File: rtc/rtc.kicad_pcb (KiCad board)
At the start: 2 copper layers, 40.4 x 36.5 mm, 14 parts, among them J1 Conn_02x03_Odd_Even, J2 Conn_01x04, J3 Conn_01x04, J4 Conn_01x04, U1 PCF8563T/5_518, Y1 LFXTAL016178REEL

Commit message: rtc pcb iteration 2
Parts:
- C1, C3: value C -> 24p; moved to B.Cu
- C2, D2, R1, R2, R3, U1, Y1: moved to B.Cu
- J1: footprint Connector_PinHeader_2.54mm:PinHeader_2x03_P2.54mm_Vertical -> Connector_PinSocket_2.54mm:PinSocket_2x03_P2.54mm_Vertical; moved to B.Cu
- J2, J3, J4: footprint pcb_footprints:JST_SH_BM04B-SRSS-TB_1x04-1MP_P1.00mm_Vertical -> pcb_footprints:SM04BSRSSTB; moved to B.Cu
- moved C3 87.7 mm to (152.3, 76.1), turned to 135 degrees
- moved C1 84.2 mm to (147.0, 81.1), turned to 135 degrees
- moved Y1 83.6 mm to (148.0, 77.0), turned to 135 degrees
- moved U1 80.7 mm to (155.9, 82.2), turned to -45 degrees
- moved R1 78.2 mm to (161.4, 93.3), turned to -135 degrees
- moved C2 74.5 mm to (156.6, 89.6)
- moved SUPERCAP1 72.1 mm to (161.6, 88.5), turned to -45 degrees
- moved D2 71.2 mm to (157.9, 92.9), turned to -135 degrees
- moved R2 69.3 mm to (152.0, 89.0), turned to -90 degrees
- moved R3 69.2 mm to (154.5, 89.0), turned to -90 degrees
- moved J2 64.1 mm to (160.0, 70.7), turned to 0 degrees
- moved J3 62.8 mm to (161.2, 78.3)
- moved J1 62.5 mm to (154.5, 98.5)
- moved J4 53.2 mm to (150.8, 70.7), turned to 0 degrees
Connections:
- J1 pad 1: +3.3V -> GND
- J1 pad 2: unconnected-(J1-Pin_2-Pad2) -> scl
- J1 pad 3: sda -> unconnected-(J1-Pin_3-Pad3)
- J1 pad 4: unconnected-(J1-Pin_4-Pad4) -> sda
- J1 pad 5: scl -> unconnected-(J1-Pin_5-Pad5)
- J1 pad 6: GND -> +3.3V
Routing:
- net GND: track 0.00 -> 71.1 mm, vias 2 -> 9
- net Net-(SUPERCAP1-+): track 18.3 -> 4.40 mm
- net sda: track 52.1 -> 44.9 mm, vias 3 -> 0
- net Net-(U1-OSCI): track 11.1 -> 6.65 mm
- net scl: track 50.6 -> 47.8 mm, vias 5 -> 0
- net Net-(U1-OSCO): track 7.89 -> 6.35 mm
- net +3.3V: track 55.1 -> 54.9 mm, vias 3 -> 4
- removed copper zone on F.Cu, net GND
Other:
- board size 40.4 x 36.5 mm -> 23.5 x 32.4 mm
- board text removed: "3V3"
- board text removed: "GND"
- board text removed: "SCL"
- board text removed: "SDA"

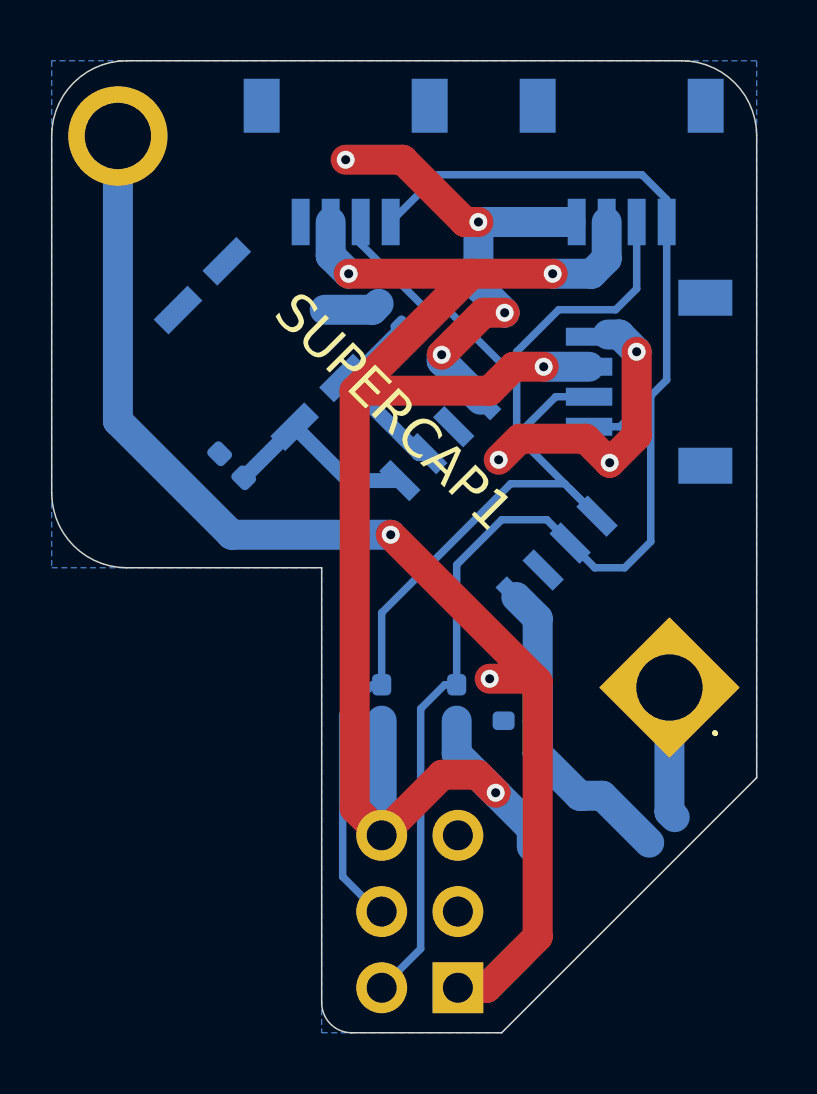
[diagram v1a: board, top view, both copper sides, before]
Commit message: finished rtc board + sensor base 3d model change
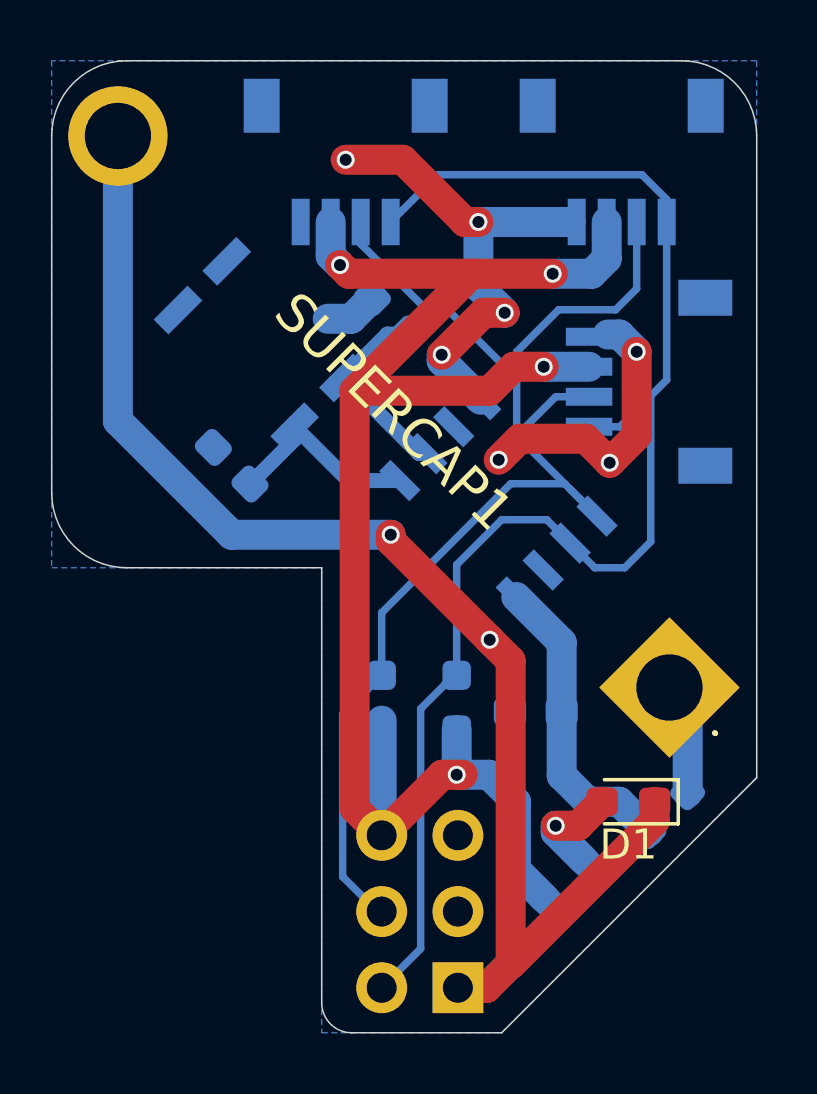
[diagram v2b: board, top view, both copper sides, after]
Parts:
- added D1: LED, LED_SMD:LED_0603_1608Metric_Pad1.05x0.95mm_HandSolder, F.Cu at (160.2, 92.3)
- added G***: LOGO, LOGO, B.Cu at (143.2, 79.7)
- added R4: 2.5k, Resistor_SMD:R_0603_1608Metric_Pad0.98x0.95mm_HandSolder, B.Cu at (158.1, 94.9)
- C1, C2, C3: footprint Capacitor_SMD:C_0402_1005Metric_Pad0.74x0.62mm_HandSolder -> Capacitor_SMD:C_0603_1608Metric_Pad1.08x0.95mm_HandSolder
- R1, R2, R3: footprint Resistor_SMD:R_0402_1005Metric_Pad0.72x0.64mm_HandSolder -> Resistor_SMD:R_0603_1608Metric_Pad0.98x0.95mm_HandSolder
- moved R1 0.67 mm to (161.6, 92.6)
- moved D2 0.67 mm to (157.7, 92.3), turned to 180 degrees
- moved C2 0.59 mm to (157.1, 89.3)
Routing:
- net GND: track 71.1 -> 76.1 mm
- net Net-(D1-A): track 0.00 -> 3.43 mm, vias 0 -> 1
- net +3.3V: track 54.9 -> 55.8 mm
- net Net-(SUPERCAP1-+): track 4.40 -> 3.76 mm
- net scl: track 47.8 -> 48.3 mm
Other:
- board text added: "Designed by A. Ai"
